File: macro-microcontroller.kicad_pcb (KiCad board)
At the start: 2 copper layers, 66 x 45.7 mm, 15 parts, among them J1 Conn_01x03_Pin, J2 Conn_01x02_Pin, SW1 SW_Push, SW2 SW_Push, SW3 SW_Push, U1 XIAO-RP2040-DIP

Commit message: Rename switches as SW
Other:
- board text added: "2"
- board text added: "3"
- board text added: "Key SW1"
- board text added: "Key SW2"
- board text added: "Key SW3"
- board text added: "SW1"
- board text added: "SW1/IO2"
- board text added: "SW2/IO3"
- board text added: "SW3/IO4"
- board text removed: "Key S1"
- board text removed: "Key S2"
- board text removed: "Key S3"
- board text removed: "S1"
- board text removed: "S1/IO2"
- board text removed: "S2"
- board text removed: "S2/IO3"
- board text removed: "S3"
- board text removed: "S3/IO4"
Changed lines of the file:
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@@
 		)
 	)
-	(gr_text "S1/IO2"
+	(gr_text "SW1/IO2"
 		(at 132.08 69.342 0)
 		(layer "F.SilkS")
@@
 		)
 	)
-	(gr_text "Key S3"
+	(gr_text "Key SW3"
 		(at 159.512 109.728 0)
 		(layer "F.SilkS")
@@
 		)
 	)
-	(gr_text "S2"
+	(gr_text "2"
 		(at 133.096 83.058 0)
 		(layer "F.SilkS")
@@
 		)
 	)
-	(gr_text "S1"
+	(gr_text "SW1"
 		(at 130.556 83.058 0)
 		(layer "F.SilkS")
@@
 		)
 	)
-	(gr_text "Key S1"
+	(gr_text "Key SW1"
 		(at 116.84 109.728 0)
 		(layer "F.SilkS")
@@
 		)
 	)
-	(gr_text "S2/IO3"
+	(gr_text "SW2/IO3"
 		(at 139.954 69.342 0)
 		(layer "F.SilkS")
@@
 		)
 	)
-	(gr_text "Key S2"
+	(gr_text "Key SW2"
 		(at 138.176 109.728 0)
 		(layer "F.SilkS")
@@
 		)
 	)
-	(gr_text "S3\n"
+	(gr_text "3\n"
 		(at 135.636 83.058 0)
 		(layer "F.SilkS")
@@
 		)
 	)
-	(gr_text "S3/IO4"
+	(gr_text "SW3/IO4"
 		(at 147.828 69.342 0)
 		(layer "F.SilkS")

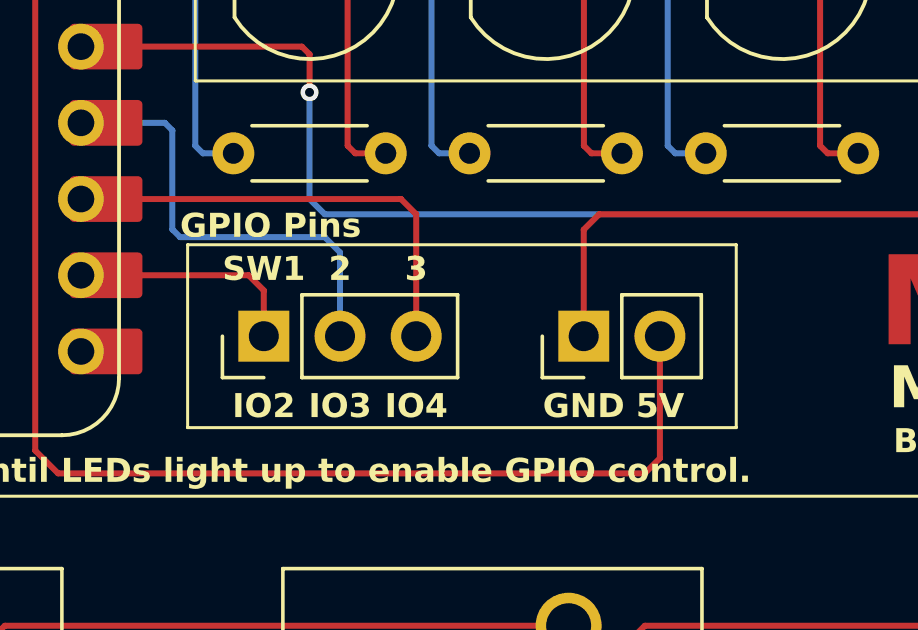
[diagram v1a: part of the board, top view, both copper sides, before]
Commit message: Update GPIO pin labels
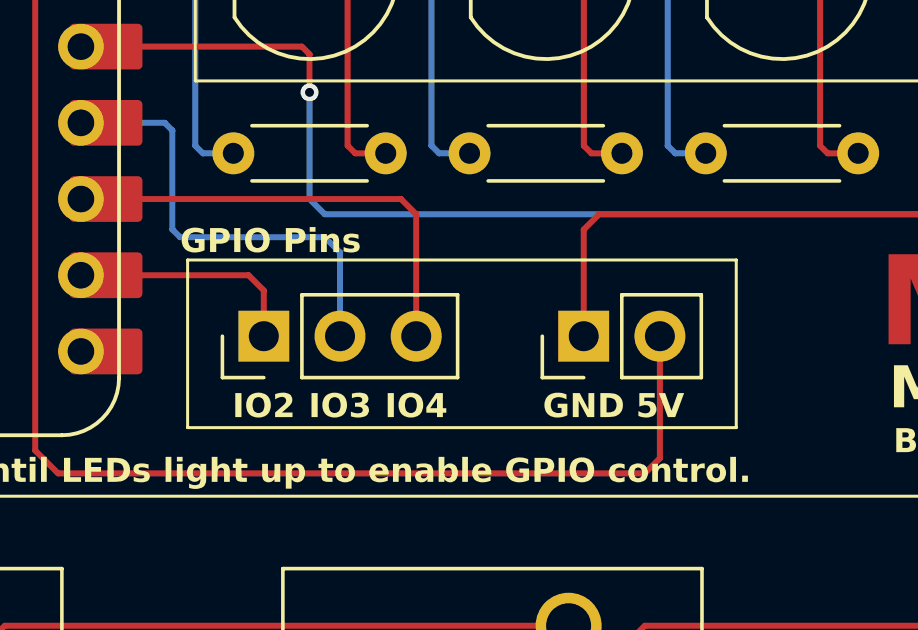
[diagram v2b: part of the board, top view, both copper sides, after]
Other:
- board text removed: "2"
- board text removed: "3"
- board text removed: "SW1"
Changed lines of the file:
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@@
 	)
 	(gr_rect
-		(start 128.016 81.788)
+		(start 128.016 82.296)
 		(end 146.304 87.884)
 		(stroke
@@
 		)
 	)
-	(gr_text "2"
-		(at 133.096 83.058 0)
-		(layer "F.SilkS")
-		(effects
-			(font
-				(size 0.8 0.8)
-				(thickness 0.16)
-				(bold yes)
-			)
-			(justify bottom)
-		)
-	)
-	(gr_text "SW1"
-		(at 130.556 83.058 0)
-		(layer "F.SilkS")
-		(effects
-			(font
-				(size 0.8 0.8)
-				(thickness 0.16)
-				(bold yes)
-			)
-			(justify bottom)
-		)
-	)
 	(gr_text "Press & hold any key until LEDs light up to enable GPIO control."
 		(at 107.188 89.789 0)
@@
 	)
 	(gr_text "GPIO Pins"
-		(at 127.762 81.153 0)
+		(at 127.762 81.661 0)
 		(layer "F.SilkS")
 		(effects
@@
 				(bold yes)
 			)
-			(justify bottom)
-		)
-	)
-	(gr_text "3\n"
-		(at 135.636 83.058 0)
-		(layer "F.SilkS")
-		(effects
-			(font
-				(size 0.8 0.8)
-				(thickness 0.16)
-				(bold yes)
-			)

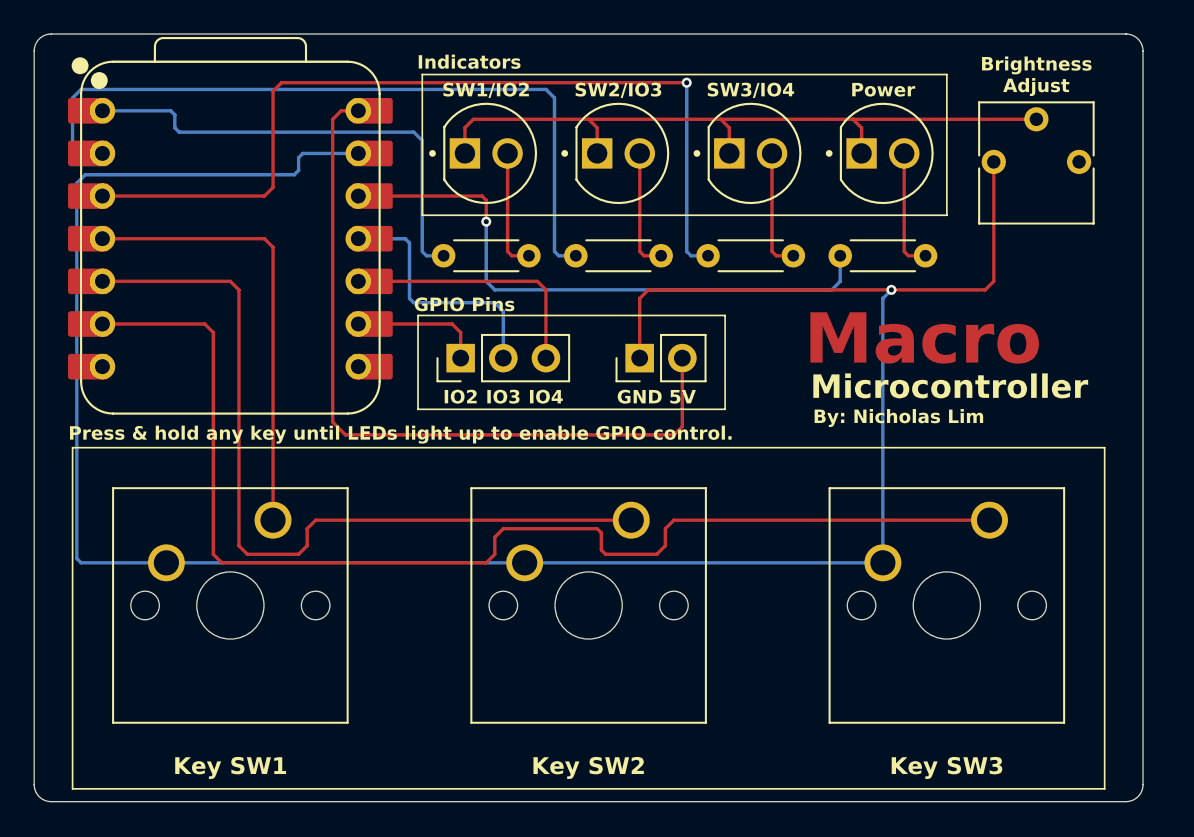
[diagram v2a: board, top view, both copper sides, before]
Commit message: Move GPIO pin placement
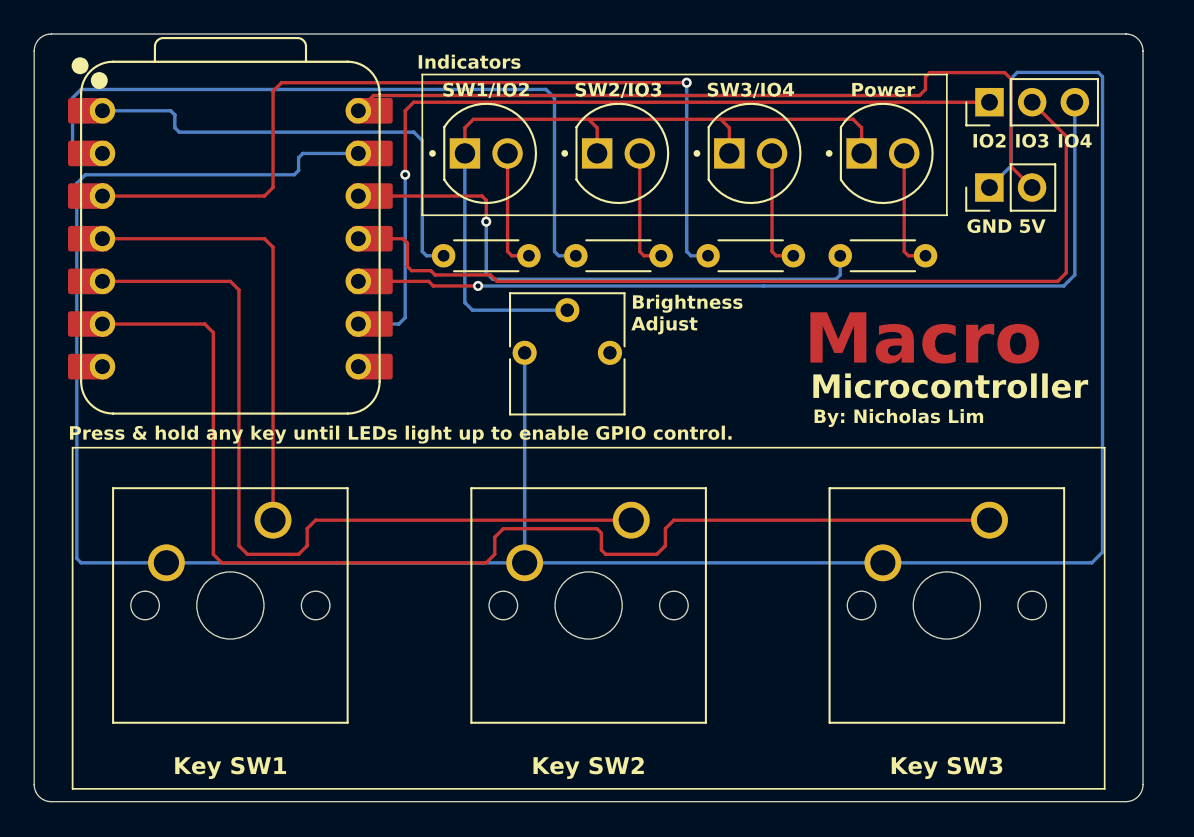
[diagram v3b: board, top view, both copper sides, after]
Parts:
- moved J1 35.0 mm to (162.1, 69.6)
- moved RV1 30.2 mm to (139.4, 84.5)
- moved J2 23.2 mm to (162.0, 74.7)
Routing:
- net IO2: track 7.00 -> 50.3 mm, vias 0 -> 1
- net IO3: track 15.2 -> 55.2 mm
- net IO4: track 15.5 -> 53.3 mm, vias 0 -> 1
- net GND: track 137.0 -> 155.3 mm, vias 1 -> 0
- net Adjusted GND: track 42.5 -> 46.7 mm
- net +5V: track 46.0 -> 47.4 mm
- net Power: track 34.7 -> 33.7 mm
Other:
- board text removed: "GPIO Pins"

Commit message: Add ground plane
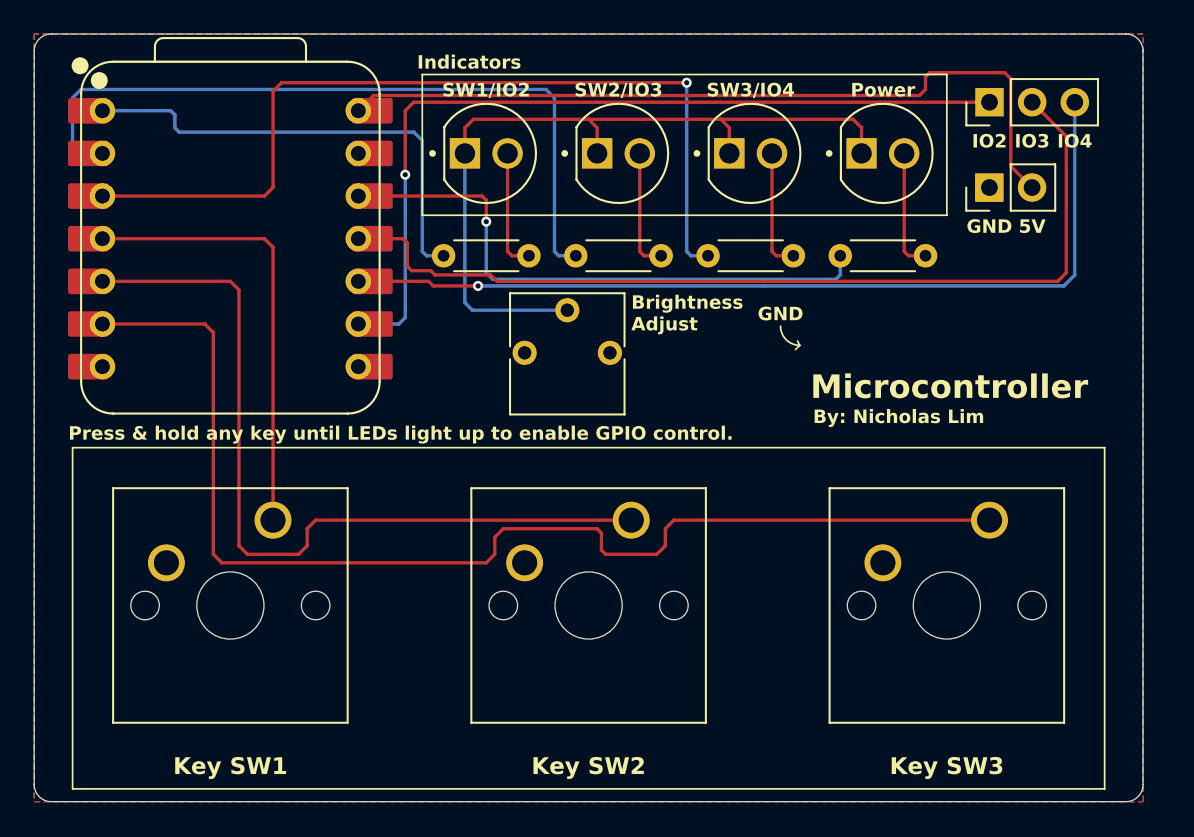
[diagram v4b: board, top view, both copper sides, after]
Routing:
- net GND: track 155.3 -> 0.00 mm
- added copper zone on B.Cu, net GND
- added copper zone on F.Cu, net GND
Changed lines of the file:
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@@
+		(layer "F.SilkS")
+	)
+	(gr_line
+		(start 150.749 84.074)
+		(end 150.495 84.328)
+		(stroke
+			(width 0.1)
+			(type default)
+		)
+		(layer "F.SilkS")
+	)
+	(gr_arc
+		(start 150.749 84.074)
+		(mid 149.940777 83.739223)
+		(end 149.606 82.931)
+		(stroke
+			(width 0.1)
+			(type default)
+		)
+		(layer "F.SilkS")
+	)
+	(gr_line
+		(start 150.749 84.074)
+		(end 150.622 83.82)
+		(stroke
+			(width 0.1)
+			(type default)
+		)
 		(layer "F.SilkS")
 	)
@@
 	(gr_text "Macro"
 		(at 151.003 85.471 0)
-		(layer "F.Cu")
+		(layer "F.Mask")
 		(effects
 			(font
@@
 		)
 	)
-	(gr_text "Macro"
-		(at 151.003 85.471 0)
-		(layer "F.Mask")
-		(effects
-			(font
-				(size 3 3)
-				(thickness 0.6)
-				(bold yes)
-			)
-			(justify left bottom)
-		)
-	)
 	(gr_text "SW1/IO2"
 		(at 132.08 69.342 0)
@@
 	)
 	(gr_text "GND"
+		(at 149.606 82.677 0)
+		(layer "F.SilkS")
+		(effects
+			(font
+				(size 0.8 0.8)
+				(thickness 0.16)
+				(bold yes)
+			)
+			(justify bottom)
+		)
+	)
+	(gr_text "GND"
 		(at 162.047 77.47 0)
 		(layer "F.SilkS")
@@
 	)
 	(segment
-		(start 120.904 73.66)
-		(end 120.65 73.914)
-		(width 0.2)
-		(layer "B.Cu")
-		(net 1)
-	)
-	(segment
-		(start 163.322 73.406)
-		(end 163.322 68.199)
-		(width 0.2)
-		(layer "B.Cu")
-		(net 1)
-	)
-	(segment
-		(start 107.696 96.774)
-		(end 107.95 97.028)
-		(width 0.2)
-		(layer "B.Cu")
-		(net 1)
-	)
-	(segment
-		(start 168.148 97.028)
-		(end 155.702 97.028)
-		(width 0.2)
-		(layer "B.Cu")
-		(net 1)
-	)
-	(segment
-		(start 107.696 74.422)
-		(end 107.696 96.774)
-		(width 0.2)
-		(layer "B.Cu")
-		(net 1)
-	)
-	(segment
-		(start 163.322 68.199)
-		(end 163.703 67.818)
-		(width 0.2)
-		(layer "B.Cu")
-		(net 1)
-	)
-	(segment
-		(start 168.783 96.393)
-		(end 168.148 97.028)
-		(width 0.2)
-		(layer "B.Cu")
-		(net 1)
-	)
-	(segment
-		(start 120.65 73.914)
-		(end 108.204 73.914)
-		(width 0.2)
-		(layer "B.Cu")
-		(net 1)
-	)
-	(segment
-		(start 121.158 72.644)
-		(end 120.904 72.898)
-		(width 0.2)
-		(layer "B.Cu")
-		(net 1)
-	)
-	(segment
-		(start 108.204 73.914)
-		(end 107.696 74.422)
-		(width 0.2)
-		(layer "B.Cu")
-		(net 1)
-	)
-	(segment
-		(start 168.529 67.818)
-		(end 168.783 68.072)
-		(width 0.2)
-		(layer "B.Cu")
-		(net 1)
-	)
-	(segment
-		(start 134.366 97.028)
-		(end 113.03 97.028)
-		(width 0.2)
-		(layer "B.Cu")
-		(net 1)
-	)
-	(segment
-		(start 163.703 67.818)
-		(end 168.529 67.818)
-		(width 0.2)
-		(layer "B.Cu")
-		(net 1)
-	)
-	(segment
-		(start 168.783 68.072)
-		(end 168.783 96.393)
-		(width 0.2)
-		(layer "B.Cu")
-		(net 1)
-	)
-	(segment
-		(start 134.366 84.522)
-		(end 134.366 97.028)
-		(width 0.2)
-		(layer "B.Cu")
-		(net 1)
-	)
-	(segment
-		(start 120.904 72.898)
-		(end 120.904 73.66)
-		(width 0.2)
-		(layer "B.Cu")
-		(net 1)
-	)
-	(segment
-		(start 155.702 97.028)
-		(end 134.366 97.028)
-		(width 0.2)
-		(layer "B.Cu")
-		(net 1)
-	)
-	(segment
-		(start 107.95 97.028)
-		(end 113.03 97.028)
-		(width 0.2)
-		(layer "B.Cu")
-		(net 1)
-	)
-	(segment
-		(start 124.46 72.644)
-		(end 121.158 72.644)
-		(width 0.2)
-		(layer "B.Cu")
-		(net 1)
-	)
-	(segment
 		(start 162.047 74.676)
 		(end 162.052 74.676)
-		(width 0.2)
-		(layer "B.Cu")
-		(net 1)
-	)
-	(segment
-		(start 162.052 74.676)
-		(end 163.322 73.406)
 		(width 0.2)
 		(layer "B.Cu")
@@
 		(net 19)
 	)
+	(zone
+		(net 1)
+		(net_name "GND")
+		(layers "F.Cu" "B.Cu")
+		(hatch edge 0.5)
+		(connect_pads
+			(clearance 0.5)
+		)
+		(min_thickness 0.25)
+		(filled_areas_thickness no)
+		(fill yes
+			(thermal_gap 0.5)
+			(thermal_bridge_width 0.5)
+		)
+		(polygon
+			(pts
+				(xy 171.196 111.252) (xy 171.196 65.532) (xy 105.156 65.532) (xy 105.156 111.252)
+			)
+		)
+	)
 	(embedded_fonts no)

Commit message: Edit ground plane
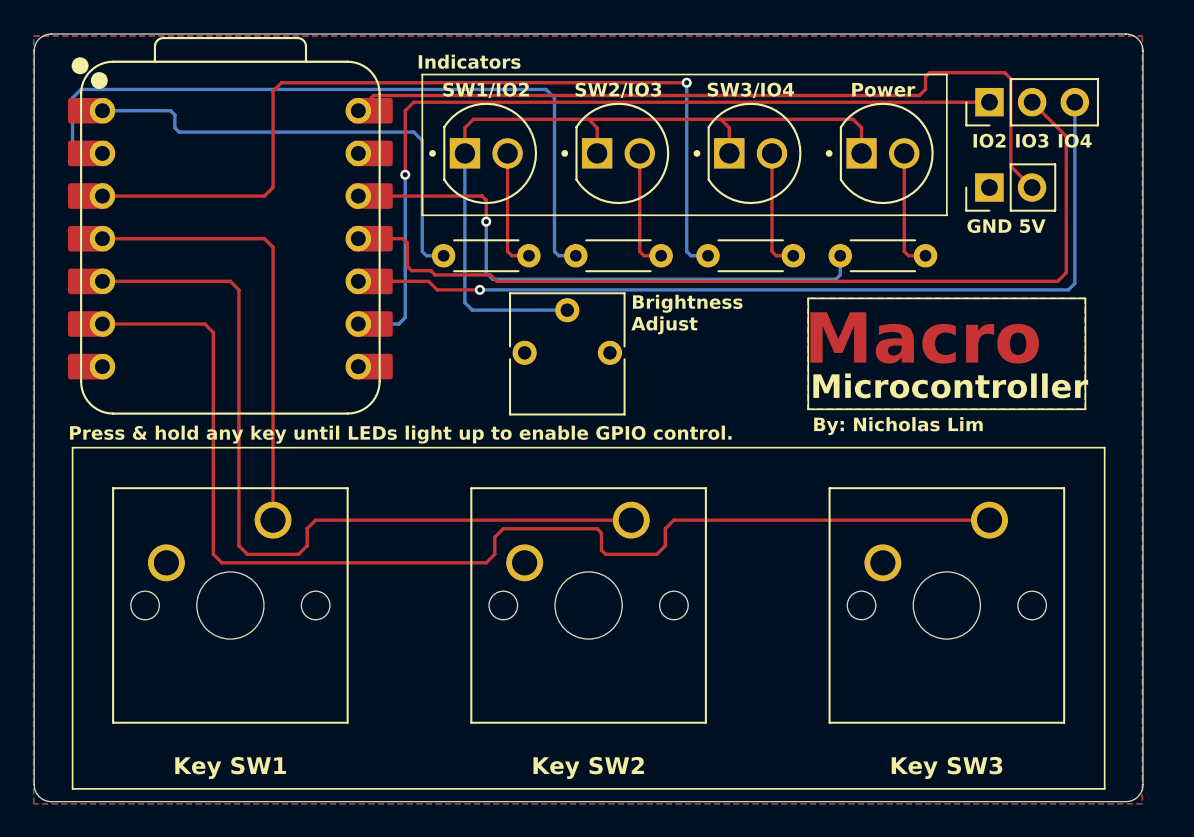
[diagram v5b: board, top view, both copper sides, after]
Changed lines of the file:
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@@
 		(layer "F.SilkS")
 	)
-	(gr_line
-		(start 150.749 84.074)
-		(end 150.495 84.328)
+	(gr_rect
+		(start 151.257 81.28)
+		(end 167.767 87.884)
 		(stroke
 			(width 0.1)
 			(type default)
 		)
-		(layer "F.SilkS")
-	)
-	(gr_arc
-		(start 150.749 84.074)
-		(mid 149.940777 83.739223)
-		(end 149.606 82.931)
-		(stroke
-			(width 0.1)
-			(type default)
-		)
-		(layer "F.SilkS")
-	)
-	(gr_line
-		(start 150.749 84.074)
-		(end 150.622 83.82)
-		(stroke
-			(width 0.1)
-			(type default)
-		)
+		(fill no)
 		(layer "F.SilkS")
 	)
@@
 	(gr_text "Macro"
 		(at 151.003 85.471 0)
-		(layer "F.Mask")
+		(layer "F.Cu")
 		(effects
 			(font
@@
 		)
 	)
+	(gr_text "Macro"
+		(at 151.003 85.471 0)
+		(layer "F.Mask")
+		(effects
+			(font
+				(size 3 3)
+				(thickness 0.6)
+				(bold yes)
+			)
+			(justify left bottom)
+		)
+	)
 	(gr_text "SW1/IO2"
 		(at 132.08 69.342 0)
@@
 	)
 	(gr_text "By: Nicholas Lim"
-		(at 151.5364 88.7984 0)
+		(at 151.511 89.281 0)
 		(layer "F.SilkS")
 		(effects
@@
 				(size 1 1)
 				(thickness 0.2)
-				(bold yes)
-			)
-			(justify bottom)
-		)
-	)
-	(gr_text "GND"
-		(at 149.606 82.677 0)
-		(layer "F.SilkS")
-		(effects
-			(font
-				(size 0.8 0.8)
-				(thickness 0.16)
 				(bold yes)
 			)
@@
 	)
 	(segment
-		(start 128.925 80.538)
-		(end 131.592 80.538)
-		(width 0.2)
-		(layer "F.Cu")
-		(net 16)
-	)
-	(segment
 		(start 124.46 80.264)
 		(end 128.651 80.264)
@@
 	(segment
 		(start 128.651 80.264)
-		(end 128.925 80.538)
+		(end 129.159 80.772)
 		(width 0.2)
 		(layer "F.Cu")
 		(net 16)
 	)
+	(segment
+		(start 129.159 80.772)
+		(end 131.699 80.772)
+		(width 0.2)
+		(layer "F.Cu")
+		(net 16)
+	)
 	(via
-		(at 131.592 80.538)
+		(at 131.699 80.772)
 		(size 0.6)
 		(drill 0.3)
@@
 	)
 	(segment
-		(start 167.132 79.883)
-		(end 166.751 80.264)
+		(start 167.132 80.391)
+		(end 167.132 69.596)
 		(width 0.2)
 		(layer "B.Cu")
@@
 	)
 	(segment
-		(start 166.751 80.264)
-		(end 166.477 80.538)
+		(start 131.699 80.772)
+		(end 166.751 80.772)
 		(width 0.2)
 		(layer "B.Cu")
@@
 	)
 	(segment
-		(start 167.132 69.596)
-		(end 167.132 79.883)
-		(width 0.2)
-		(layer "B.Cu")
-		(net 16)
-	)
-	(segment
-		(start 166.477 80.538)
-		(end 148.59 80.538)
-		(width 0.2)
-		(layer "B.Cu")
-		(net 16)
-	)
-	(segment
-		(start 148.59 80.538)
-		(end 131.592 80.538)
+		(start 166.751 80.772)
+		(end 167.132 80.391)
 		(width 0.2)
 		(layer "B.Cu")
@@
 		(polygon
 			(pts
-				(xy 171.196 111.252) (xy 171.196 65.532) (xy 105.156 65.532) (xy 105.156 111.252)
-			)
-		)
+				(xy 171.159079 111.379) (xy 105.119079 111.379) (xy 105.119079 65.659) (xy 171.159079 65.659)
+			)
+		)
+		(polygon
+			(pts
+				(xy 151.220079 81.28) (xy 151.220079 87.884) (xy 167.730079 87.884) (xy 167.730079 81.28)
+			)
+		)
+	)
+	(zone
+		(net 1)
+		(net_name "GND")
+		(layer "B.Cu")
+		(hatch edge 0.5)
+		(priority 1)
+		(connect_pads
+			(clearance 0.5)
+		)
+		(min_thickness 0.25)
+		(filled_areas_thickness no)
+		(fill yes
+			(thermal_gap 0.5)
+			(thermal_bridge_width 0.5)
+		)
+		(polygon
+			(pts
+				(xy 167.730079 87.884) (xy 167.730079 81.28) (xy 151.220079 81.28) (xy 151.220079 87.884)
+			)
+		)
